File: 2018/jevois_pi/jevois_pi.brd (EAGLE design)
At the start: 48.2 x 36.5 mm, 7 parts, among them IC1 MAX3491ECSD+, J1 TM21R-5C-88(50), J2 A-USBSA, T1 R-78E3.3-0.5, U1 TSR_1-2450

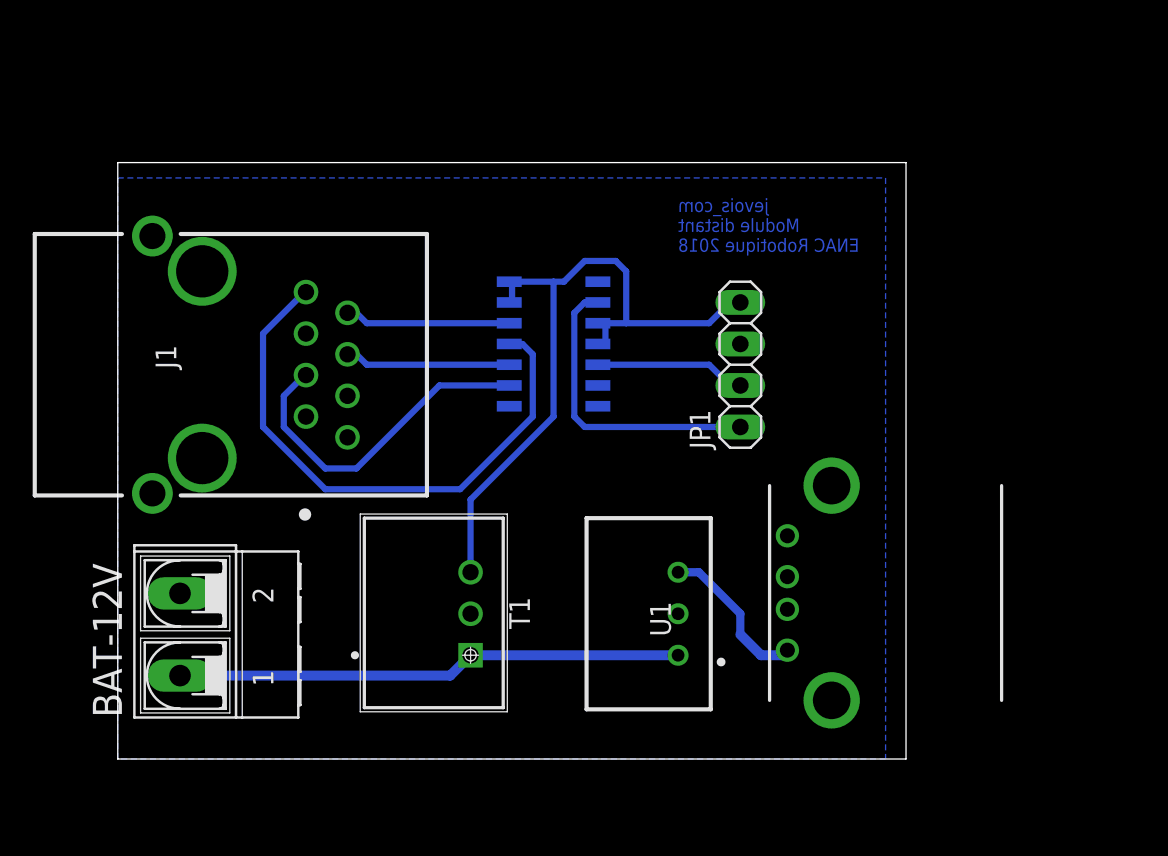
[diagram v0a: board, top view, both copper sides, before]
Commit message: Adding jevois command module and finishing boards
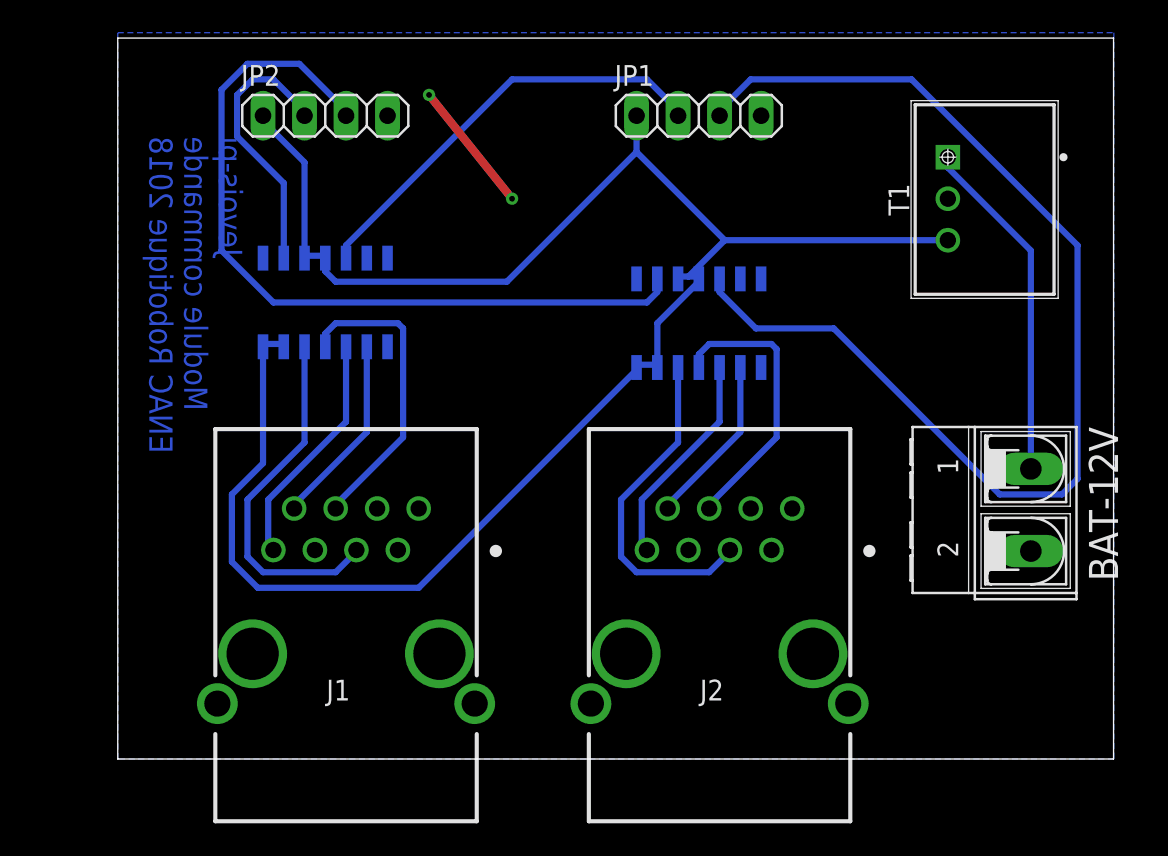
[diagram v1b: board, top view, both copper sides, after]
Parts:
- removed U1: TSR_1-2450, SamacSys_Parts:TSR-1-24120
- added IC2: MAX3491ECSD+, enac_jevois:SOIC127P600X175-14N
- added JP2: (no value), pinhead:1X04
- IC1: device SamacSys_Parts:SOIC127P600X175-14N -> enac_jevois:SOIC127P600X175-14N
- J1: device SamacSys_Parts:TM21R-5C-88(50) -> enac_jevois:TM21R-5C-88(50)
- J2: value A-USBSA -> TM21R-5C-88(50); device SamacSys_Parts:A-USBSA -> enac_jevois:TM21R-5C-88(50)
- T1: device SamacSys_Parts:SHDRV3W100P0_254_1X3_1160X850X -> enac_jevois:SHDRV3W100P0_254_1X3_1160X850X
- moved BAT-12V 52.6 mm to (55.9, 15.2), turned to 270 degrees
- moved T1 42.2 mm to (50.8, 36.8), turned to 270 degrees
- moved J1 33.8 mm to (14.0, -3.81), turned to 0 degrees
- moved J2 17.3 mm to (36.8, -3.81), turned to 0 degrees
- moved JP1 15.5 mm to (35.6, 39.4), turned to 0 degrees
- moved IC1 14.2 mm to (12.7, 27.9), turned to 270 degrees
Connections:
- net TX renamed TX1
- removed net 5V: J2.1, U1.3
- removed net N$2: BAT-12V.1, T1.1, U1.1
- removed net RX: IC1.2, JP1.1
- removed net RXA: IC1.12, J1.8
- removed net RXB: IC1.11, J1.7
- removed net TXY: IC1.9, J1.4
- removed net TXZ: IC1.10, J1.5
- new net N$3: BAT-12V.1, T1.1
- new net RX1: IC1.2, JP2.2
- new net RX1A: IC1.12, J1.4
- new net RX1B: IC1.11, J1.5
- new net RX2: IC2.2, JP2.3
- new net RX2A: IC2.12, J2.4
- new net RX2B: IC2.11, J2.5
- new net TX1Y: IC1.9, J1.8
- new net TX1Z: IC1.10, J1.7
- new net TX2: IC2.5, JP1.3
- new net TX2Y: IC2.9, J2.8
- new net TX2Z: IC2.10, J2.7
- net 3V3: now also IC2.13, IC2.14, IC2.3, IC2.4, JP1.1, JP2.1; no longer JP1.4
- net GND: now also IC2.6, IC2.7, JP1.4, JP2.4; no longer J2.4, JP1.3, U1.2
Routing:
- net 3V3: track 43.4 -> 117.4 mm
- net TX2: track 0.00 -> 69.7 mm
- net RX2: track 0.00 -> 48.7 mm
- net RXB: track 34.8 -> 0.00 mm
- net N$2: track 32.5 -> 0.00 mm
- net RX1A: track 0.00 -> 22.0 mm
- net N$3: track 0.00 -> 21.2 mm
- net TXY: track 20.7 -> 0.00 mm
- net RX2A: track 0.00 -> 20.7 mm
- net RX1B: track 0.00 -> 18.7 mm
- net RX: track 18.5 -> 0.00 mm
- net RX2B: track 0.00 -> 17.4 mm
- net TX1: track 9.24 -> 26.4 mm
- net RX1: track 0.00 -> 16.8 mm
- net TX1Z: track 0.00 -> 14.5 mm
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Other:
- board size 48.2 x 36.5 mm -> 60.9 x 44.1 mm
- board text added: "Jevois-pi Module commande ENAC Robotique 2018"
- board text removed: "jevois_com Module distant ENAC Robotique 2018"

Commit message: Correcting a mismatch between input pins
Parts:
- moved JP2 22.9 mm to (35.6, 39.4), turned to 180 degrees
- moved JP1 21.6 mm to (14.0, 39.4), turned to 180 degrees
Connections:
- net RX1: now also JP1.3; no longer JP2.2
- net TX2: now also JP2.2; no longer JP1.3
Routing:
- net RX2: track 48.7 -> 11.3 mm
- net TX1: track 26.4 -> 9.24 mm
- net 3V3: track 117.4 -> 103.5 mm
- net GND: track 8.13 -> 15.2 mm
- net RX1: track 16.8 -> 9.77 mm
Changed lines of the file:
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@@
 <autorouter>
 <pass name="Default">
-<param name="RoutingGrid" value="50mil"/>
+<param name="RoutingGrid" value="12.5mil"/>
 <param name="AutoGrid" value="1"/>
 <param name="Efforts" value="0"/>
@@
 <attribute name="SUPPLIER_NAME" value="RS" x="36.83" y="-3.81" size="1.778" layer="27" display="off"/>
 </element>
-<element name="JP1" library="pinhead" library_urn="urn:adsk.eagle:library:325" package="1X04" package3d_urn="urn:adsk.eagle:package:22407/2" value="" x="35.56" y="39.37"/>
-<element name="JP2" library="pinhead" library_urn="urn:adsk.eagle:library:325" package="1X04" package3d_urn="urn:adsk.eagle:package:22407/2" value="" x="12.7" y="39.37"/>
+<element name="JP1" library="pinhead" library_urn="urn:adsk.eagle:library:325" package="1X04" package3d_urn="urn:adsk.eagle:package:22407/2" value="" x="13.97" y="39.37" rot="R180"/>
+<element name="JP2" library="pinhead" library_urn="urn:adsk.eagle:library:325" package="1X04" package3d_urn="urn:adsk.eagle:package:22407/2" value="" x="35.56" y="39.37" rot="R180"/>
 <element name="T1" library="enac_jevois" package="SHDRV3W100P0_254_1X3_1160X850X" value="R-78E3.3-0.5" x="50.8" y="36.83" rot="R270">
 <attribute name="3D_PACKAGE" value="" x="50.8" y="36.83" size="1.778" layer="27" rot="R270" display="off"/>
@@
 <contactref element="JP1" pad="1"/>
 <contactref element="JP2" pad="1"/>
-<wire x1="12.7" y1="30.7975" x2="11.43" y2="30.7975" width="0.381" layer="16"/>
-<wire x1="12.7" y1="30.7975" x2="12.7" y2="30.652" width="0.381" layer="16"/>
-<wire x1="11.43" y1="36.5125" x2="11.43" y2="30.7975" width="0.381" layer="16"/>
-<wire x1="8.89" y1="39.0525" x2="11.43" y2="36.5125" width="0.381" layer="16"/>
-<wire x1="8.89" y1="39.37" x2="8.89" y2="39.0525" width="0.381" layer="16"/>
-<wire x1="11.43" y1="30.7975" x2="11.43" y2="30.652" width="0.381" layer="16"/>
-<wire x1="10.16" y1="25.4" x2="8.89" y2="25.4" width="0.381" layer="16"/>
+<wire x1="10.16" y1="25.4" x2="9.525" y2="25.4" width="0.381" layer="16"/>
+<wire x1="9.525" y1="25.4" x2="8.89" y2="25.4" width="0.381" layer="16"/>
 <wire x1="8.89" y1="25.4" x2="8.89" y2="25.228" width="0.381" layer="16"/>
 <wire x1="10.16" y1="25.4" x2="10.16" y2="25.228" width="0.381" layer="16"/>
@@
 <wire x1="31.75" y1="23.8125" x2="18.415" y2="10.4775" width="0.381" layer="16"/>
 <wire x1="31.75" y1="23.8125" x2="31.75" y2="23.958" width="0.381" layer="16"/>
-<wire x1="37.1475" y1="31.75" x2="50.8" y2="31.75" width="0.381" layer="16"/>
+<wire x1="37.1475" y1="31.75" x2="39.37" y2="31.75" width="0.381" layer="16"/>
+<wire x1="39.37" y1="31.75" x2="50.8" y2="31.75" width="0.381" layer="16"/>
 <wire x1="34.925" y1="29.5275" x2="37.1475" y2="31.75" width="0.381" layer="16"/>
-<wire x1="31.75" y1="37.1475" x2="31.75" y2="39.37" width="0.381" layer="16"/>
-<wire x1="37.1475" y1="31.75" x2="31.75" y2="37.1475" width="0.381" layer="16"/>
-<wire x1="12.7" y1="29.845" x2="12.7" y2="30.652" width="0.381" layer="16"/>
-<wire x1="13.335" y1="29.21" x2="12.7" y2="29.845" width="0.381" layer="16"/>
-<wire x1="23.8125" y1="29.21" x2="13.335" y2="29.21" width="0.381" layer="16"/>
-<wire x1="31.75" y1="37.1475" x2="23.8125" y2="29.21" width="0.381" layer="16"/>
+<wire x1="12.7" y1="29.21" x2="12.7" y2="30.652" width="0.381" layer="16"/>
+<wire x1="12.7" y1="30.7975" x2="11.43" y2="30.7975" width="0.381" layer="16"/>
+<wire x1="11.43" y1="30.7975" x2="11.43" y2="30.652" width="0.381" layer="16"/>
+<wire x1="12.7" y1="30.7975" x2="12.7" y2="30.652" width="0.381" layer="16"/>
+<wire x1="12.7" y1="28.575" x2="12.7" y2="29.21" width="0.381" layer="16"/>
+<wire x1="9.525" y1="25.4" x2="12.7" y2="28.575" width="0.381" layer="16"/>
+<wire x1="17.78" y1="29.845" x2="17.78" y2="39.37" width="0.381" layer="16"/>
+<wire x1="17.145" y1="29.21" x2="17.78" y2="29.845" width="0.381" layer="16"/>
+<wire x1="12.7" y1="29.21" x2="17.145" y2="29.21" width="0.381" layer="16"/>
+<wire x1="39.37" y1="31.75" x2="39.37" y2="39.37" width="0.381" layer="16"/>
 </signal>
 <signal name="GND">
@@
 <vertex x="60.96" y="0"/>
 </polygon>
-<via x="24.13" y="34.29" extent="1-16" drill="0.35"/>
-<via x="19.05" y="40.64" extent="1-16" drill="0.35"/>
-<wire x1="19.05" y1="40.64" x2="24.13" y2="34.29" width="0.508" layer="1"/>
+<via x="44.45" y="35.56" extent="1-16" drill="0.35"/>
+<via x="29.21" y="35.56" extent="1-16" drill="0.35"/>
+<wire x1="29.21" y1="35.56" x2="44.45" y2="35.56" width="0.508" layer="1"/>
 </signal>
 <signal name="RX1">
 <contactref element="IC1" pad="2"/>
-<contactref element="JP2" pad="2"/>
-<wire x1="10.16" y1="35.2425" x2="10.16" y2="30.652" width="0.381" layer="16"/>
-<wire x1="7.3025" y1="38.1" x2="10.16" y2="35.2425" width="0.381" layer="16"/>
-<wire x1="7.3025" y1="40.64" x2="7.3025" y2="38.1" width="0.381" layer="16"/>
-<wire x1="8.255" y1="41.5925" x2="7.3025" y2="40.64" width="0.381" layer="16"/>
-<wire x1="9.525" y1="41.5925" x2="8.255" y2="41.5925" width="0.381" layer="16"/>
-<wire x1="11.43" y1="39.6875" x2="9.525" y2="41.5925" width="0.381" layer="16"/>
-<wire x1="11.43" y1="39.37" x2="11.43" y2="39.6875" width="0.381" layer="16"/>
+<contactref element="JP1" pad="3"/>
+<wire x1="10.16" y1="36.5125" x2="10.16" y2="30.652" width="0.381" layer="16"/>
+<wire x1="12.7" y1="39.0525" x2="10.16" y2="36.5125" width="0.381" layer="16"/>
+<wire x1="12.7" y1="39.37" x2="12.7" y2="39.0525" width="0.381" layer="16"/>
 </signal>
 <signal name="TX1">
 <contactref element="IC1" pad="5"/>
 <contactref element="JP1" pad="2"/>
-<wire x1="13.97" y1="31.4325" x2="13.97" y2="30.652" width="0.381" layer="16"/>
-<wire x1="24.13" y1="41.5925" x2="13.97" y2="31.4325" width="0.381" layer="16"/>
-<wire x1="32.385" y1="41.5925" x2="24.13" y2="41.5925" width="0.381" layer="16"/>
-<wire x1="34.29" y1="39.6875" x2="32.385" y2="41.5925" width="0.381" layer="16"/>
-<wire x1="34.29" y1="39.37" x2="34.29" y2="39.6875" width="0.381" layer="16"/>
+<wire x1="13.97" y1="37.7825" x2="13.97" y2="30.652" width="0.381" layer="16"/>
+<wire x1="15.24" y1="39.0525" x2="13.97" y2="37.7825" width="0.381" layer="16"/>
+<wire x1="15.24" y1="39.37" x2="15.24" y2="39.0525" width="0.381" layer="16"/>
 </signal>
 <signal name="RX2">
@@
 <contactref element="JP2" pad="3"/>
 <wire x1="33.02" y1="28.575" x2="33.02" y2="29.382" width="0.381" layer="16"/>
-<wire x1="32.385" y1="27.94" x2="33.02" y2="28.575" width="0.381" layer="16"/>
-<wire x1="9.525" y1="27.94" x2="32.385" y2="27.94" width="0.381" layer="16"/>
-<wire x1="6.35" y1="31.115" x2="9.525" y2="27.94" width="0.381" layer="16"/>
-<wire x1="6.35" y1="40.9575" x2="6.35" y2="31.115" width="0.381" layer="16"/>
-<wire x1="7.9375" y1="42.545" x2="6.35" y2="40.9575" width="0.381" layer="16"/>
-<wire x1="11.1125" y1="42.545" x2="7.9375" y2="42.545" width="0.381" layer="16"/>
-<wire x1="13.97" y1="39.6875" x2="11.1125" y2="42.545" width="0.381" layer="16"/>
-<wire x1="13.97" y1="39.37" x2="13.97" y2="39.6875" width="0.381" layer="16"/>
+<wire x1="33.02" y1="37.7825" x2="33.02" y2="29.382" width="0.381" layer="16"/>
+<wire x1="34.29" y1="39.0525" x2="33.02" y2="37.7825" width="0.381" layer="16"/>
+<wire x1="34.29" y1="39.37" x2="34.29" y2="39.0525" width="0.381" layer="16"/>
 </signal>
 <signal name="TX2">
 <contactref element="IC2" pad="5"/>
-<contactref element="JP1" pad="3"/>
 <wire x1="36.83" y1="28.575" x2="36.83" y2="29.382" width="0.381" layer="16"/>
+<contactref element="JP2" pad="2"/>
 <wire x1="39.0525" y1="26.3525" x2="36.83" y2="28.575" width="0.381" layer="16"/>
 <wire x1="43.815" y1="26.3525" x2="39.0525" y2="26.3525" width="0.381" layer="16"/>
